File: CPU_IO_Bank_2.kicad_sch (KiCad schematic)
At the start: 5 parts, among them U3 SPC5676RDK3MVU1R

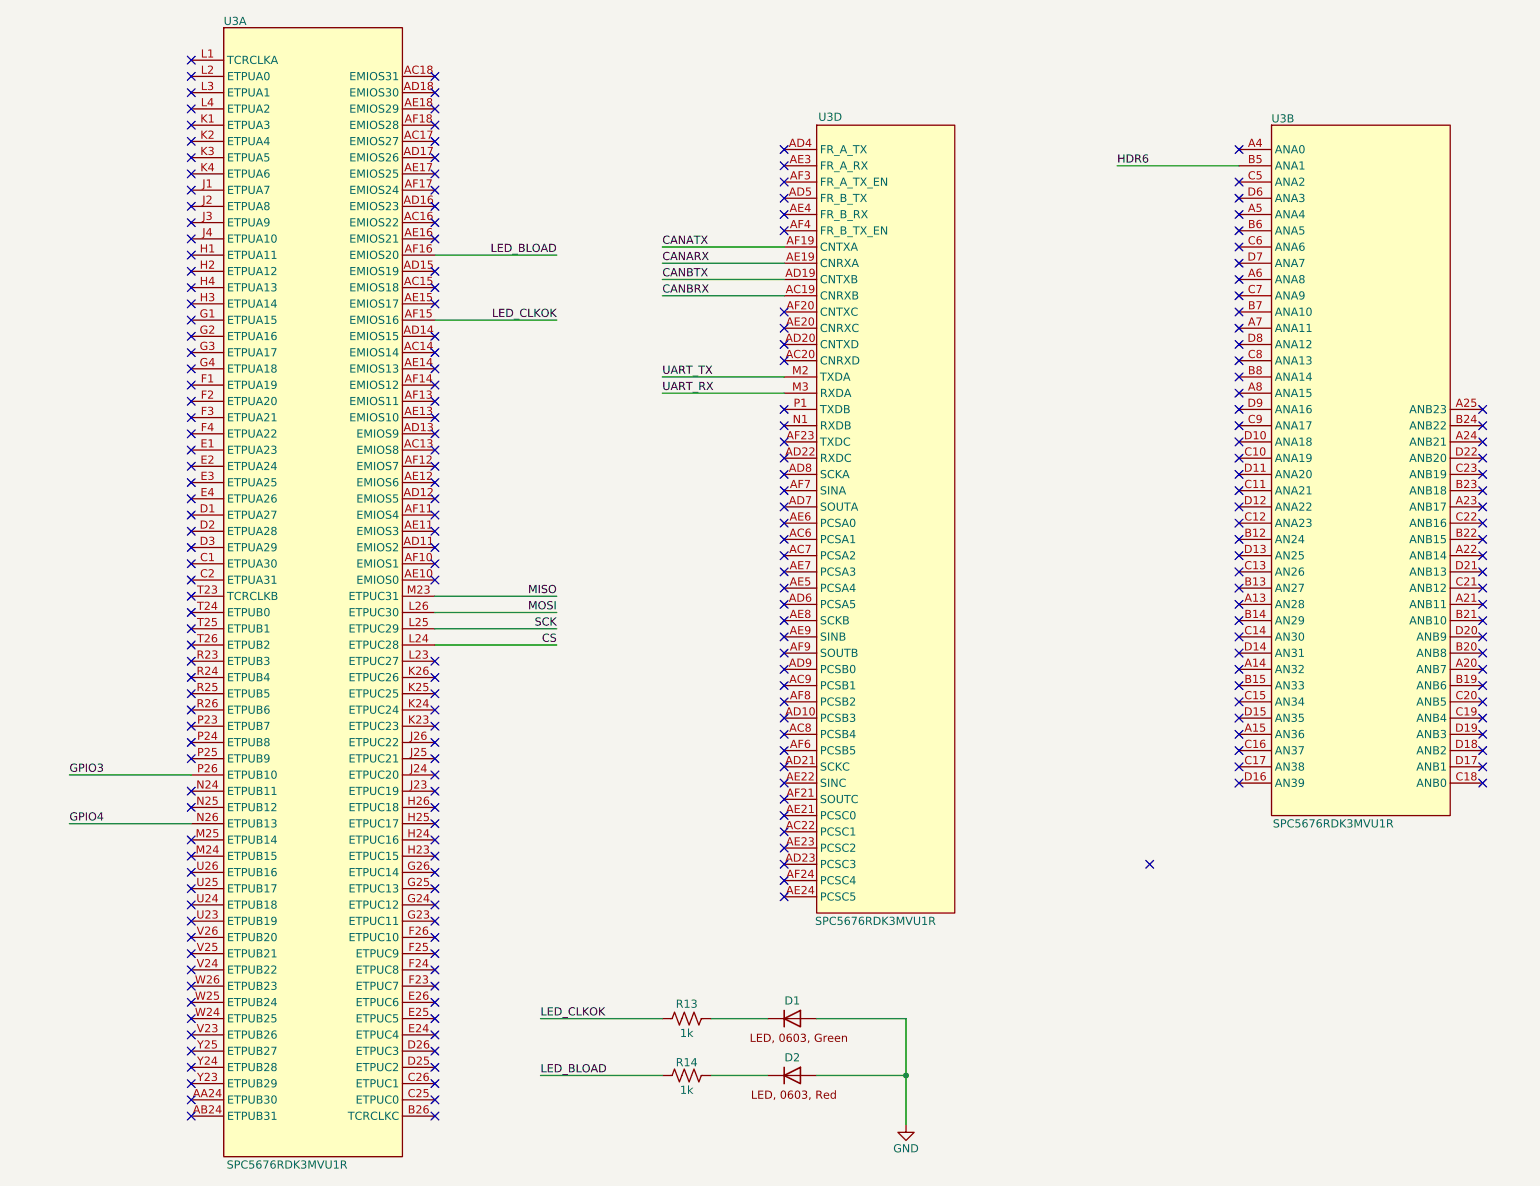
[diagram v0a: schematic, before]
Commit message: draft updated, schematic draft done, pcb issues with size of board and fitting all parts on
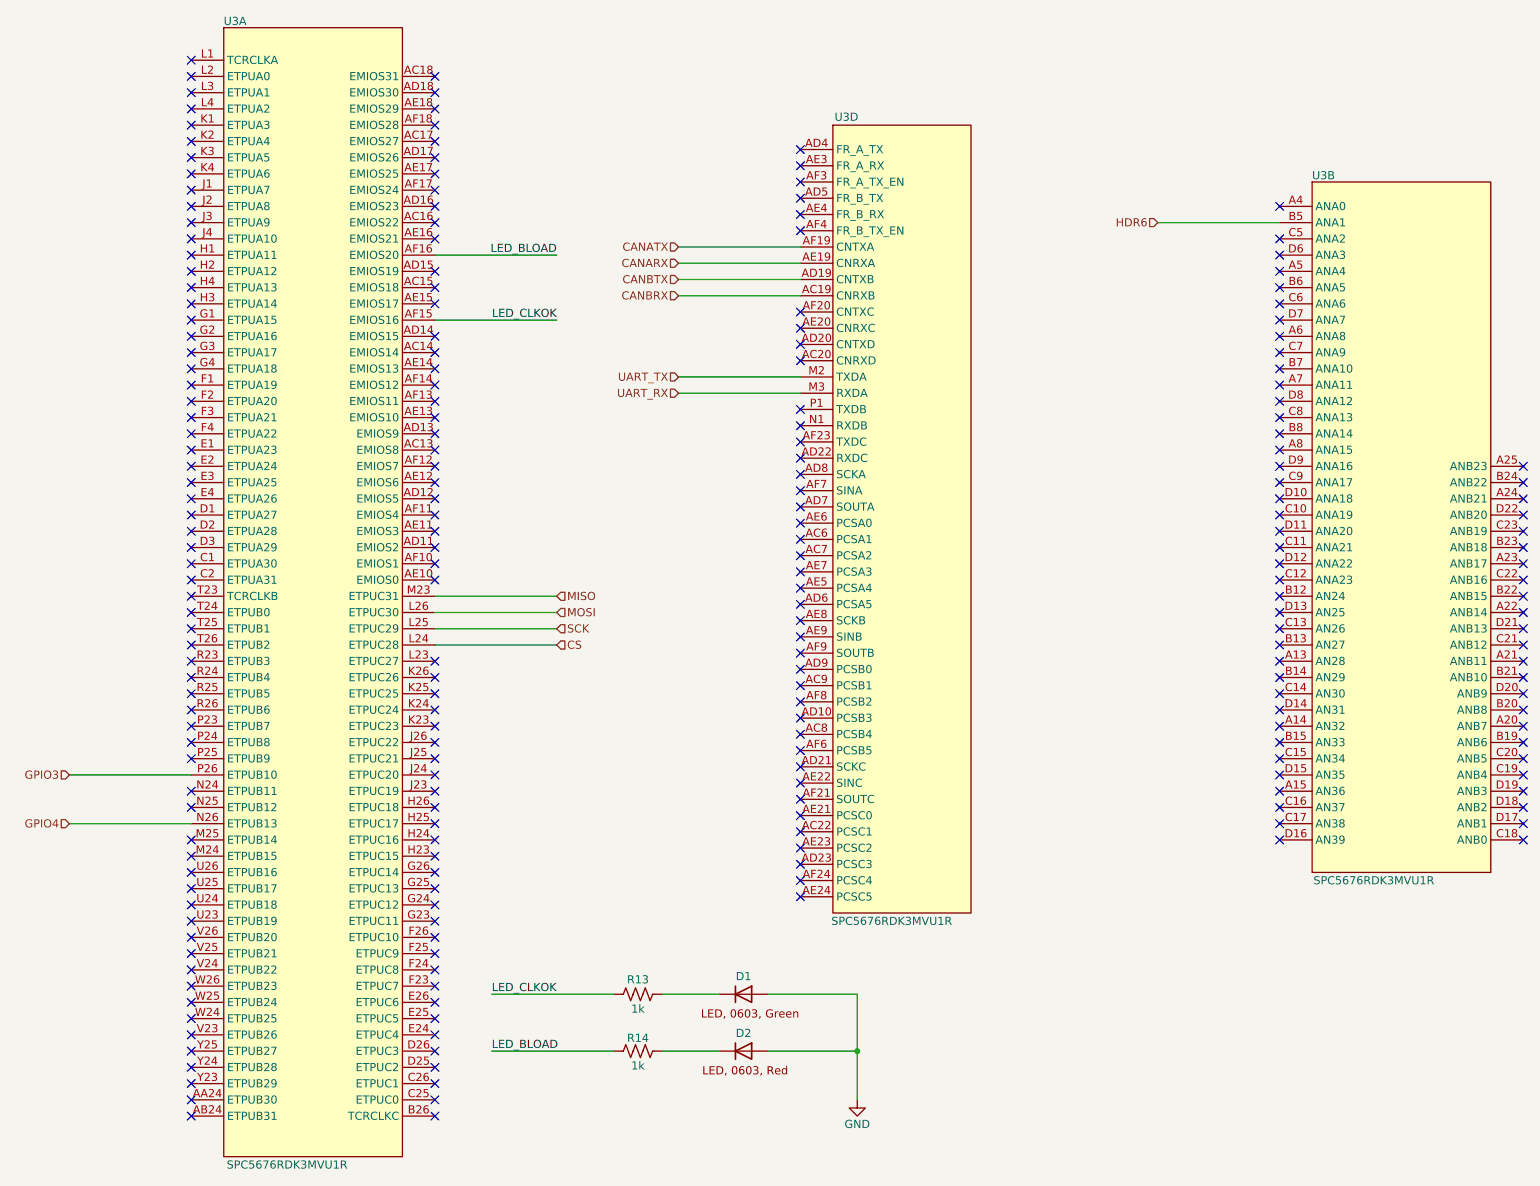
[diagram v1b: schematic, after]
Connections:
- no-connect marks 228 -> 227
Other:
- moved on the sheet: D1, D2, R13, R14, U3B, U3D

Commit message: updated schematic after library re-organization
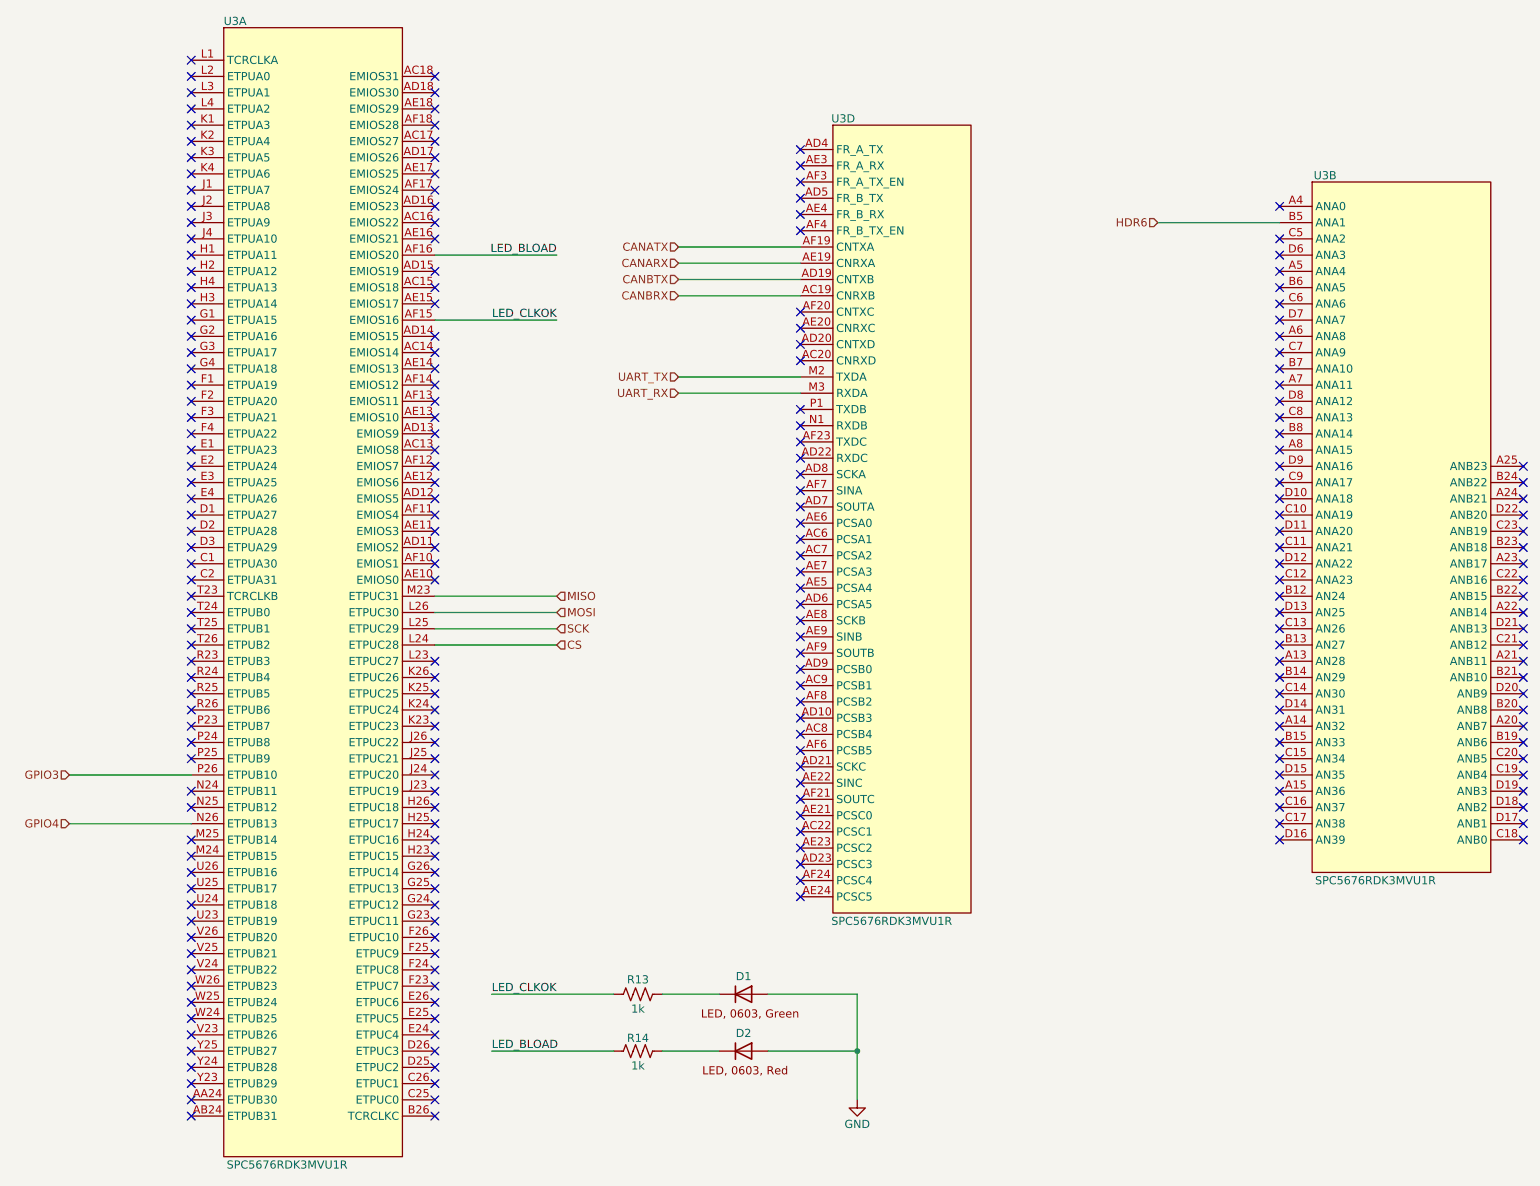
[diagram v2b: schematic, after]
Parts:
- removed D1: APT1608SRCPRV, LED_SMD:LED_0603_1608Metric, symbol tutorial_2_library:APT1608SRCPRV_Green
- removed D2: APT1608SRCPRV, LED_SMD:LED_0603_1608Metric, symbol tutorial_2_library:APT1608SRCPRV_Red
- removed U3: SPC5676RDK3MVU1R, tutorial_2_library:BGA416C100P26X26_2700X2700X255N, symbol tutorial_2_library:SPC5676RDK3MVU1R
- added D1: APT1608SRCPRV, LED_SMD:LED_0603_1608Metric, symbol NAE_Diodes:APT1608SRCPRV_Green
- added D2: APT1608SRCPRV, LED_SMD:LED_0603_1608Metric, symbol NAE_Diodes:APT1608SRCPRV_Red
- added U3: SPC5676RDK3MVU1R, tutorial_2_library:BGA416C100P26X26_2700X2700X255N, symbol NAE_Integrated_Circuits:SPC5676RDK3MVU1R
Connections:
- net CANARX: now also U3.AE19 (CNRXA)
- net CANATX: now also U3.AF19 (CNTXA)
- net CANBRX: now also U3.AC19 (CNRXB)
- net CANBTX: now also U3.AD19 (CNTXB)
- net CS: now also U3.L24 (ETPUC28)
- net GND: now also D1.2, D2.2
- net GPIO3: now also U3.P26 (ETPUB10)
- net GPIO4: now also U3.N26 (ETPUB13)
- net HDR6: now also U3.B5 (ANA1)
- net LED_BLOAD: now also U3.AF16 (EMIOS20)
- net LED_CLKOK: now also U3.AF15 (EMIOS16)
- net MISO: now also U3.M23 (ETPUC31)
- net MOSI: now also U3.L26 (ETPUC30)
- net SCK: now also U3.L25 (ETPUC29)
- net UART_RX: now also U3.M3 (RXDA)
- net UART_TX: now also U3.M2 (TXDA)
- net at R14.2: now also D2.1
- net at R13.2: now also D1.1
